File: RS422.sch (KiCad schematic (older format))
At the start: 11 parts, among them J1 L77SDA15S1ACH4F, J2 Conn_01x05_Male, J3 Conn_01x05_Male, J4 Conn_01x01_Male, U1 AM26LV32xD, U2 AM26LV32xD

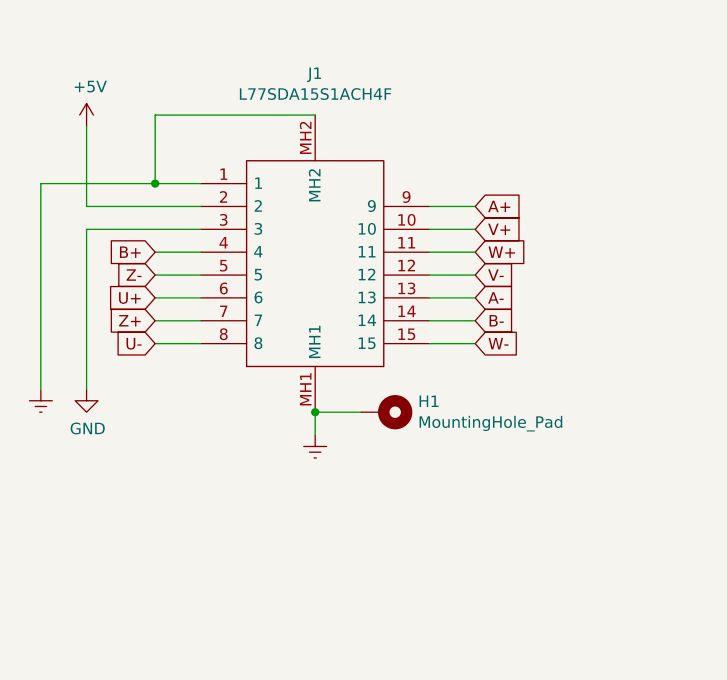
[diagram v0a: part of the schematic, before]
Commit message: Added Mige encoder cable colors
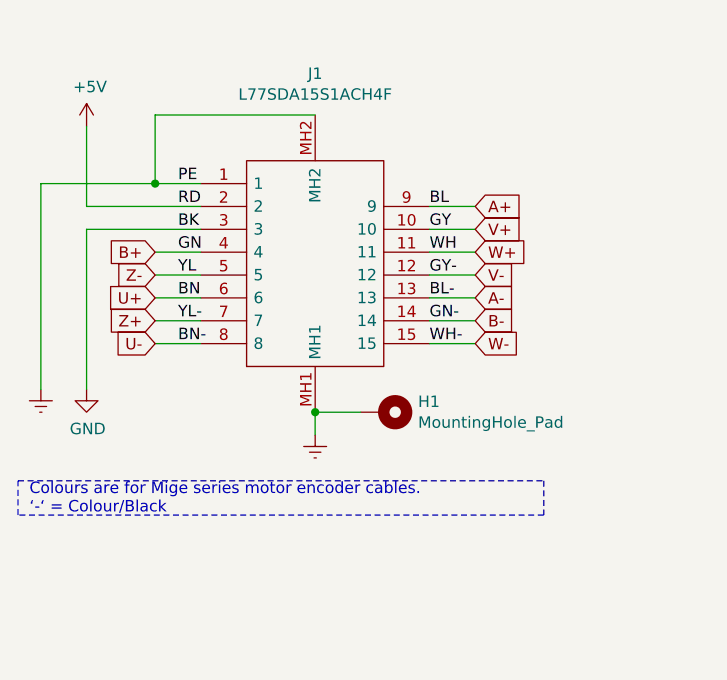
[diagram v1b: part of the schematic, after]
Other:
- note added: "Colours are for Mige series motor encoder cables. \n‘-‘ = Colour/Black"
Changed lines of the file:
@@
 $EndComp
 Connection ~ 7950 2450
+Text Label 2200 3300 0    50   ~ 0
+RD
+Text Label 2200 3400 0    50   ~ 0
+BK
+Text Label 2200 3500 0    50   ~ 0
+GN
+Text Label 2200 3600 0    50   ~ 0
+YL
+Text Label 2200 3700 0    50   ~ 0
+BN
+Text Label 2200 3800 0    50   ~ 0
+YL-
+Text Label 2200 3900 0    50   ~ 0
+BN-
+Text Label 3300 3300 0    50   ~ 0
+BL
+Text Label 3300 3400 0    50   ~ 0
+GY
+Text Label 3300 3500 0    50   ~ 0
+WH
+Text Label 3300 3600 0    50   ~ 0
+GY-
+Text Label 3300 3700 0    50   ~ 0
+BL-
+Text Label 3300 3800 0    50   ~ 0
+GN-
+Text Label 3300 3900 0    50   ~ 0
+WH-
+Text Label 2200 3200 0    50   ~ 0
+PE
+Text Notes 1550 4650 0    50   ~ 0
+Colours are for Mige series motor encoder cables. \n‘-‘ = Colour/Black
+Wire Notes Line
+	1500 4500 3800 4500
+Wire Notes Line
+	3800 4500 3800 4650
+Wire Notes Line
+	3800 4650 1500 4650
+Wire Notes Line
+	1500 4650 1500 4500
 $EndSCHEMATC
